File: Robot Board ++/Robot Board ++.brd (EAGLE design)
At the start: 68.6 x 76.2 mm, 127 parts, among them U5 TPS5331[8/9].DQP

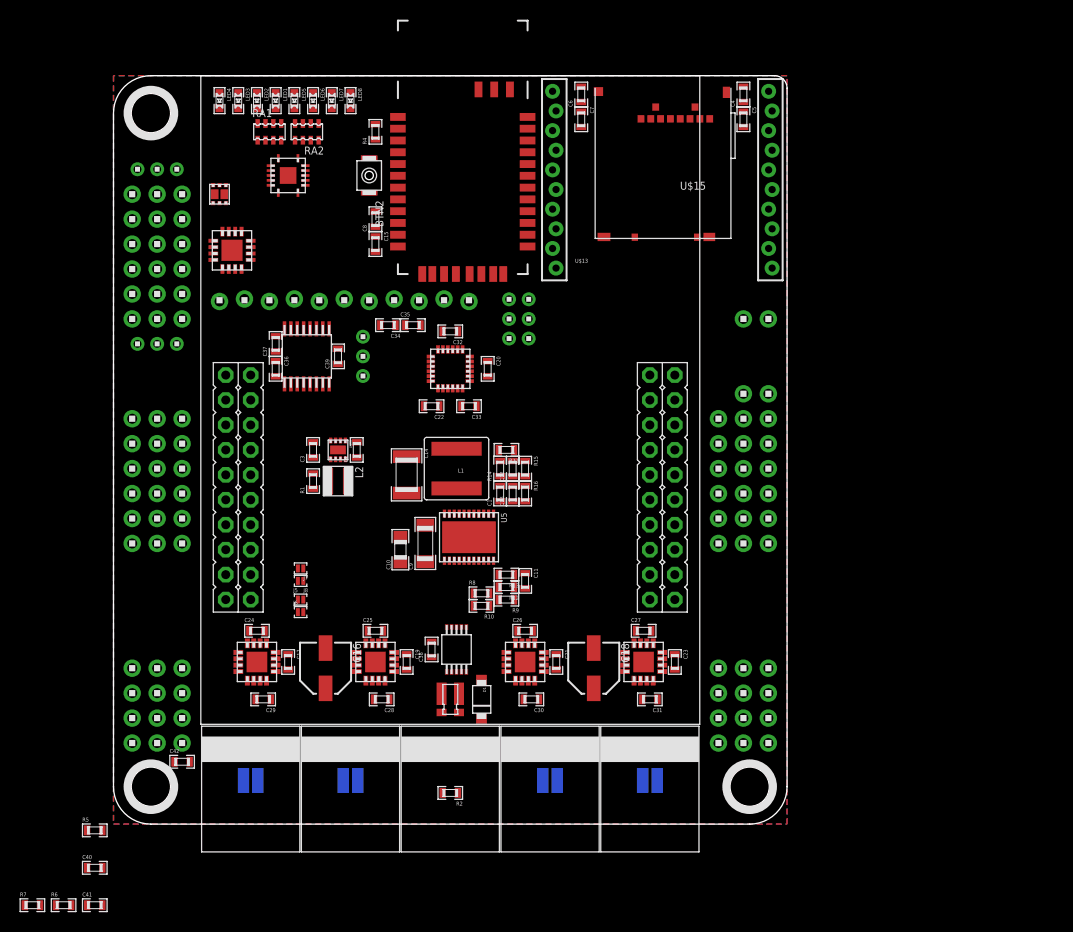
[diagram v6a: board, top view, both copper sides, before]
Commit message: Fixed Mosfet connections in Schematic Fixed 3.3v rail in Shcematic (3.3v meant to be decoupled between boards) Began routing signals on PCB
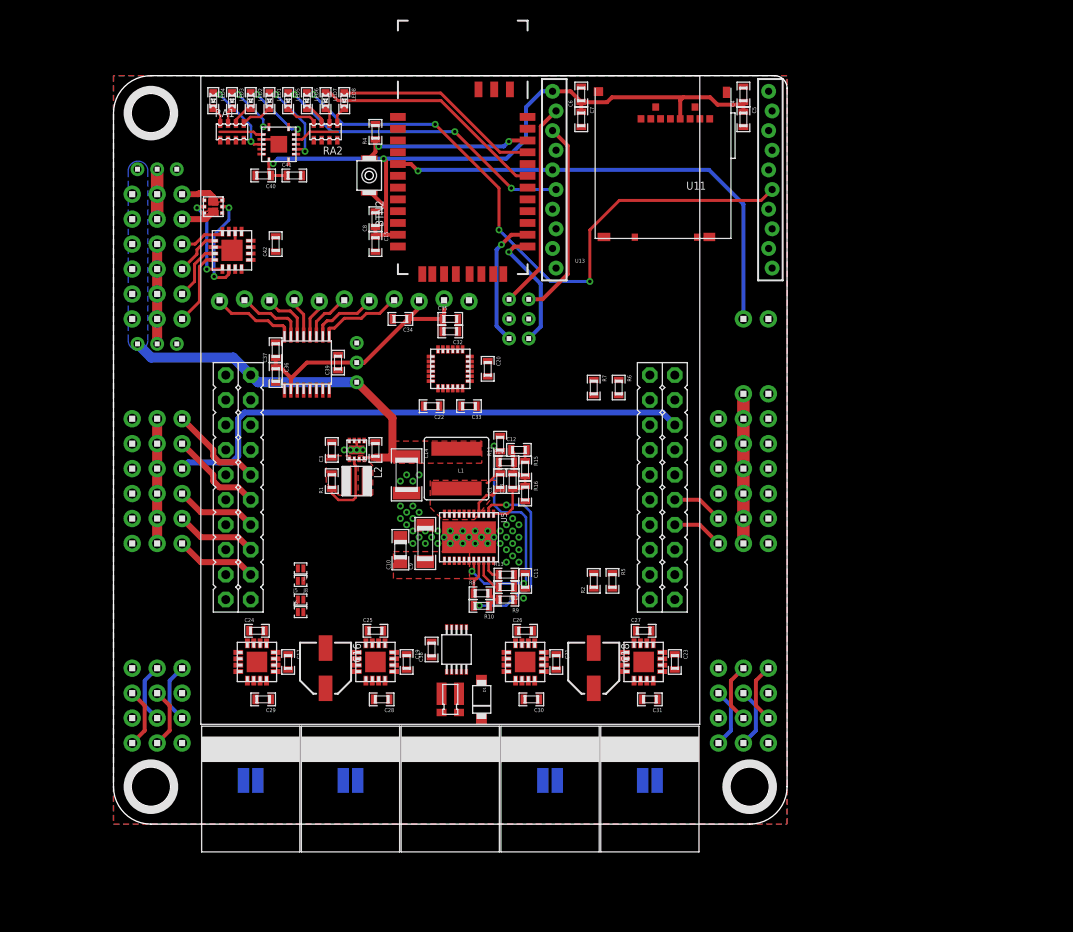
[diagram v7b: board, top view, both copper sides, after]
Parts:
- removed U$126: ADS7830.PW, packages(ti):PW.16
- removed U$132: 74XX125.RGY, packages(ti):RGY.14
- removed U$95: TPS62082.DSG, packages(ti):DSG
- added U10: 74XX125.RGY, packages(ti):RGY.14
- added U6: TPS62082.DSG, packages(ti):DSG
- added U9: ADS7830.PW, packages(ti):PW.16
- moved R7 77.7 mm to (48.9, 44.5), turned to 270 degrees
- moved R6 77.3 mm to (51.4, 44.5), turned to 270 degrees
- moved C41 77.0 mm to (18.4, 66.0)
- moved C40 72.5 mm to (15.2, 66.0), turned to 180 degrees
- moved R5 58.5 mm to (50.8, 24.8), turned to 270 degrees
- moved C42 53.6 mm to (16.5, 59.1), turned to 90 degrees
- moved R2 26.1 mm to (48.9, 24.8), turned to 90 degrees
- moved C35 3.86 mm to (34.3, 51.4)
- moved RA1 3.81 mm to (12.1, 70.5)
- moved H9 2.54 mm to (6.99, 64.1), turned to 270 degrees
- moved C12 2.01 mm to (41.3, 38.1), turned to 0 degrees
- moved C2 1.91 mm to (26.7, 38.1)
- moved C3 1.91 mm to (22.2, 38.1)
- moved L2 1.91 mm to (24.8, 34.9)
- moved R1 1.91 mm to (22.2, 34.9)
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- renumbered U$123 to U7, U$13 to U13, U$14 to U12, U$15 to U11, U$59 to U8, U$61 to H28
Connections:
- removed net FET0: H9.1, U$55.2, U7.9
- removed net FET1: H9.2, U$55.5, U7.10
- removed net N$45: LED8.P$2, RA2.2
- removed net SVRO4: H3.5
- removed net SVRO5: H3.6
- new net FET0.D: H9.1, U$55.6, U$55.PAD@1
- new net FET0.G: U$55.2, U7.9
- new net FET1.D: H9.2, U$55.3, U$55.PAD@2
- new net FET1.G: U$55.5, U7.10
- new net N$1: U$8.3.3V
- new net N$9: LED8.P$2, RA2.1
- net 3.3V: now also U10.14, U6.5, U9.16; no longer U$126.16, U$132.14, U$8.3.3V, U$95.5
- net 3.3V.PG: now also U10.12, U6.6; no longer U$132.12, U$95.6
- net 5.0V: now also U6.8; no longer U$95.8
- net 5V.PG: now also U10.9, U6.1; no longer U$132.9, U$95.1
- net GND: now also RA2.2, U10.1, U10.10, U10.13, U10.4, U10.7, U10.PAD, U6.2, U6.3, U6.PAD, U9.11, U9.12, U9.13, U9.9; no longer RA2.1, U$126.11, U$126.12, U$126.13, U$126.9, U$132.1, U$132.10, U$132.13, U$132.4, U$132.7, U$132.PAD, U$95.2, U$95.3, U$95.PAD
- net I2C.SDA: now also U9.15; no longer U$126.15
- net I2C.SDL: now also U9.14; no longer U$126.14
- net LS.1: now also U9.1; no longer U$126.1
- net LS.2: now also U9.2; no longer U$126.2
- net LS.3: now also U9.3; no longer U$126.3
- net LS.4: now also U9.4; no longer U$126.4
- net LS.5: now also U9.5; no longer U$126.5
- net LS.6: now also U9.6; no longer U$126.6
- net LS.7: now also U9.7; no longer U$126.7
- net LS.8: now also U9.8; no longer U$126.8
- net N$12: now also U6.7; no longer U$95.7
- net N$43: now also U10.6; no longer U$132.6
- net N$44: now also U10.11; no longer U$132.11
- net N$50: now also U10.8; no longer U$132.8
- net N$6: now also U10.3; no longer U$132.3
- net SVRO4/ENC2.!CS: now also H3.5
- net SVRO5/ENC3.!CS: now also H3.6
- net UART.RXI: now also U10.5; no longer U$132.5
- net UART.TXO: now also U10.2; no longer U$132.2
- net VCC: now also U9.10; no longer U$126.10
- net VIN: no longer U$55.6, U$55.PAD@1
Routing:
- net 3.3V: track 0.00 -> 88.1 mm, vias 0 -> 2
- net XBEE.ASSOCIATE: track 0.00 -> 64.8 mm, vias 0 -> 4
- net AD3: track 0.00 -> 55.3 mm
- net 5.0V: track 0.00 -> 54.0 mm
- net !RST: track 0.00 -> 48.6 mm, vias 0 -> 1
- net XBEE.RSSI: track 0.00 -> 31.3 mm, vias 0 -> 3
- net VCC: track 0.00 -> 26.5 mm
- net N$4: track 0.00 -> 25.0 mm, vias 0 -> 3
- net BT.STATUS: track 0.00 -> 24.1 mm
- net VDDIO: track 0.00 -> 22.4 mm
- net BT.CONNECT: track 0.00 -> 21.2 mm
- net XBEE.RXI: track 0.00 -> 21.2 mm
- net XBEE.TXO: track 0.00 -> 20.3 mm
- net N$8: track 0.00 -> 19.5 mm, vias 0 -> 2
- net BT.RESET: track 0.00 -> 18.1 mm, vias 0 -> 2
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- added copper zone on layer 1, net 3.3V
- added copper zone on layer 1, net 5.0V
- added copper zone on layer 16, net 5.0V
- added copper zone on layer 1, net FET0.D
- added copper zone on layer 1, net FET1.D
- added copper zone on layer 1, net N$12
- added copper zone on layer 1, net N$15
- added copper zone on layer 1, net VBAT
